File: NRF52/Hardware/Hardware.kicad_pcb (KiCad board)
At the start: 2 copper layers, 33 x 38.1 mm, 81 parts, among them J1 USB_C_Receptacle_USB2.0, J2 1.54 E-INK, J3 Conn_01x04, J4 Battery, Q1 AO3401A, Q2 AO3400A, Q3 AO3400A, Q4 AO3401A, SW1 SW_Push, SW2 SW_Push, SW3 SW_Push, U1 nRF52840, U2 TP4054, U3 BQ27441DRZR-G1A, U4 XC6206PxxxMR, U5 LSM6DS3, U6 DS3231MZ, Y1 32MHz 8pF ±10ppm, Y2 32.768kHz 6pF ±20ppm

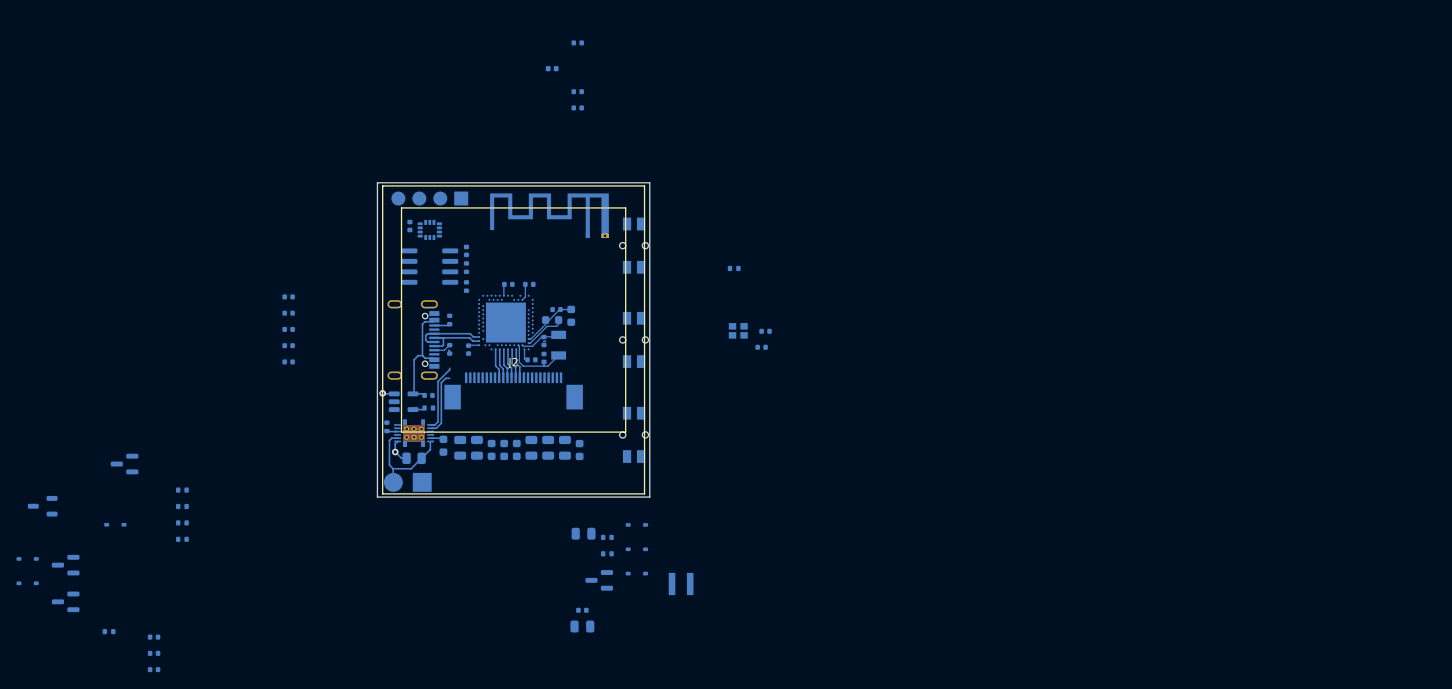
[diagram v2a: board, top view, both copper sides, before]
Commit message: NRF52 hardware as ordered
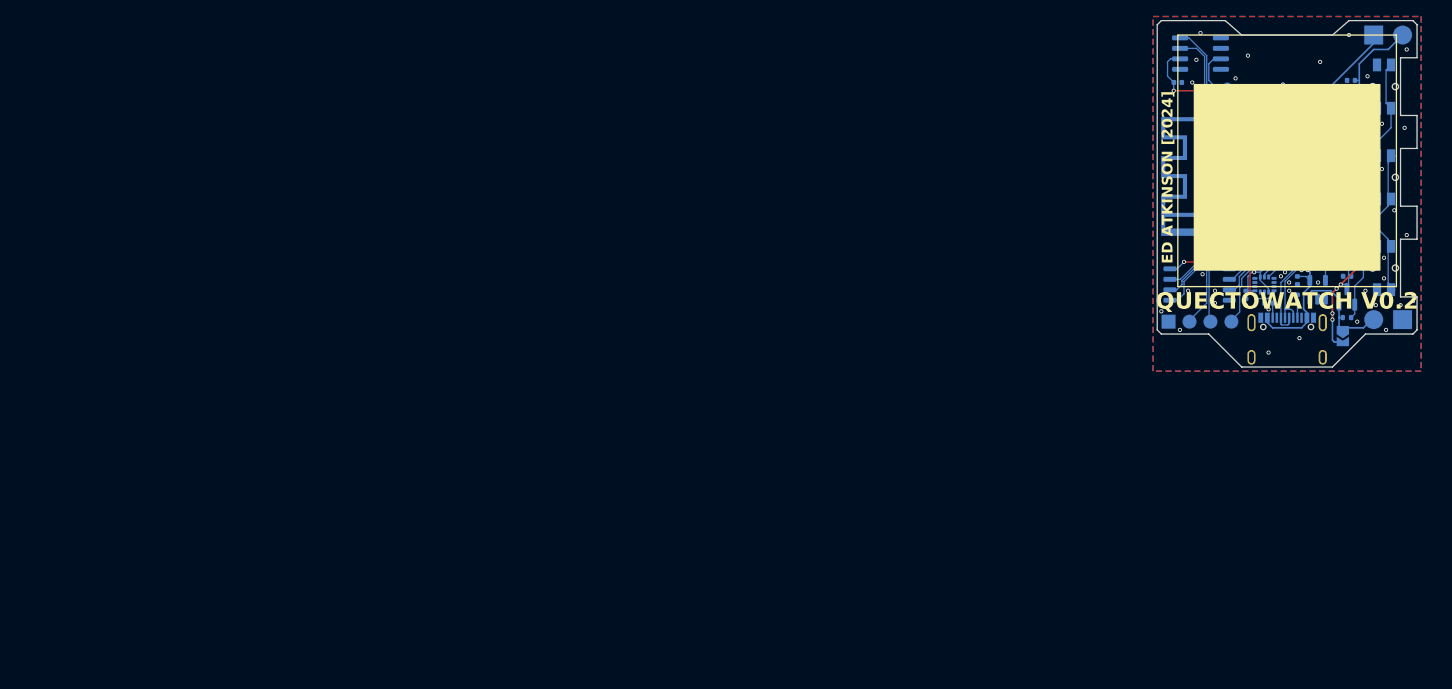
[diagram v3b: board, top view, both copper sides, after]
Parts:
- removed C23, C26, C27, C30: 1u, Capacitor_SMD:C_0603_1608Metric
- removed C24, C25, C28, C29: 4u7, Capacitor_SMD:C_0805_2012Metric
- removed C32: 470n, Capacitor_SMD:C_0603_1608Metric
- removed C33: 100n, Capacitor_SMD:C_0402_1005Metric
- removed D2, D3, D4, D5, D6: 1N5819WS, Diode_SMD:D_SOD-323
- removed L2: 10u, Inductor_SMD:L_Taiyo-Yuden_MD-3030
- removed Q3: AO3400A, Package_TO_SOT_SMD:SOT-23
- removed R12, R13: 10K, Resistor_SMD:R_0402_1005Metric
- added J5: MOTOR, local:Battery Pads, B.Cu at (207.0, 64.0)
- added JP1: SolderJumper_2_Open, Jumper:SolderJumper-2_P1.3mm_Open_TrianglePad1.0x1.5mm, B.Cu at (201.5, 100.5)
- added TP2: LCD_REFRESH, TestPoint:TestPoint_Pad_D1.0mm, B.Cu at (187.5, 70.2)
- added U7: W25Q128JVS, Package_SO:SOIC-8_5.23x5.23mm_P1.27mm, B.Cu at (184.2, 94.2)
- AE1: footprint RF_Antenna:Texas_SWRA117D_2.4GHz_Right -> local:Texas_SWRA117D_2.4GHz_Left
- C19: value 4u7 -> 100n
- C20: value 4u7 -> 100p; footprint Capacitor_SMD:C_0805_2012Metric -> Capacitor_SMD:C_0402_1005Metric
- C21, C22: value 4u7 -> 1u; footprint Capacitor_SMD:C_0805_2012Metric -> Capacitor_SMD:C_0402_1005Metric
- J2: value 1.54 E-INK -> LCD; footprint local:1.54_Epaper_Display -> Connector_FFC-FPC:Molex_54548-1071_1x10-1MP_P0.5mm_Horizontal
- J3: value Conn_01x04 -> PROG
- J4: value Battery -> BAT
- R11: value 1M -> 100K
- R5: value 10K -> 100K
- R6: value 0R47 -> 10K
- R7: value R01 1% -> 10K; footprint Resistor_SMD:R_0805_2012Metric -> Resistor_SMD:R_0402_1005Metric
- U3: value BQ27441DRZR-G1A -> MAX17048; footprint Package_SON:Texas_S-PDSO-N12 -> Package_DFN_QFN:TDFN-8-1EP_2x2mm_P0.5mm_EP0.8x1.2mm
- moved U4 166.1 mm to (202.6, 72.1), turned to -90 degrees
- moved R3 162.1 mm to (202.0, 75.0)
- moved C35 161.8 mm to (202.5, 69.5)
- moved C34 160.0 mm to (204.0, 75.0)
- moved Q4 159.7 mm to (202.0, 95.8), turned to 90 degrees
- moved D1 157.5 mm to (203.2, 77.3), turned to 90 degrees
- moved Q1 151.0 mm to (199.8, 77.2)
- moved R10 142.7 mm to (202.0, 98.2)
- moved R11 132.3 mm to (186.5, 79.8), turned to 0 degrees
- moved C12 126.8 mm to (199.8, 82.2), turned to 0 degrees
- moved C13 125.9 mm to (199.2, 88.0), turned to -90 degrees
- moved C18 121.0 mm to (192.5, 80.5), turned to 90 degrees
- moved C14 120.7 mm to (194.0, 90.0), turned to 0 degrees
- moved J4 120.5 mm to (207.0, 98.5)
- moved R8 118.2 mm to (201.5, 88.2), turned to 0 degrees
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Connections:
- C19 pad 1: +3V3 -> +BATT
- C20 pad 1: Net-(D4-A) -> +3V3
- C20 pad 2: Net-(D2-K) -> GND
- C21 pad 1: /PREVGH -> +3V3
- C22 pad 1: Net-(J2-Pin_4) -> +3V3
- J2 pad 1: unconnected-(J2-Pin_1-Pad1) -> /LCD_SCLK
- J2 pad 10: /EINK_RES -> GND
- J2 pad 2: /GDR -> /LCD_SDI
- J2 pad 3: /RESE -> /LCD_CS
- J2 pad 4: Net-(J2-Pin_4) -> /LCD_REFRESH
- J2 pad 5: Net-(J2-Pin_5) -> +3V3
- J2 pad 6: unconnected-(J2-Pin_6-Pad6) -> +3V3
- J2 pad 7: unconnected-(J2-Pin_7-Pad7) -> +3V3
- J2 pad 8: GND -> +3V3
- J2 pad 9: /EINK_BUSY -> GND
- J3 pad 2: /SWDIO -> /SWDCLK
- J3 pad 3: /SWDCLK -> /SWDIO
- J4 pad 2: Net-(J4-Pin_2) -> Net-(#FLG06-pwr)
- Q1 pad 3: Net-(Q1-D) -> +BATT
- Q2 pad 1: /GDR -> /MOTOR_EN
- Q2 pad 2: /RESE -> GND
- Q2 pad 3: Net-(D4-A) -> Net-(J5-Pin_1)
- Q4 pad 1: Net-(D5-A) -> /POWER_LATCH
- Q4 pad 2: +BATT -> Net-(#FLG06-pwr)
- Q4 pad 3: Net-(Q1-D) -> +BATT
- R10 pad 1: Net-(D5-A) -> /POWER_LATCH
- R10 pad 2: +BATT -> Net-(#FLG06-pwr)
- R11 pad 1: GND -> /MOTOR_EN
- R11 pad 2: /POWER_LATCH -> GND
- R14 pad 2: /SDA -> /RTC_SDA
- R15 pad 2: /SCL -> /RTC_SCL
- R4 pad 1: /~{RESET} -> +3V3
- R4 pad 2: +3V3 -> /IMU_SDA
- R5 pad 1: GND -> +3V3
- R5 pad 2: /GDR -> /LCD_REFRESH
- R6 pad 1: GND -> +3V3
- R6 pad 2: /RESE -> /IMU_SCL
- R7 pad 1: Net-(J4-Pin_2) -> +3V3
- R7 pad 2: +BATT -> /FG_SDA
- R8 pad 1: Net-(U3-BIN) -> +3V3
- R8 pad 2: GND -> /FG_SCL
- SW1 pad 1: GND -> /MENU_BUTTON
- SW1 pad 2: Net-(D5-K) -> GND
- U1 pad A10: unconnected-(U1-AIN5/P0.29-PadA10) -> /LCD_SDI
- U1 pad A12: unconnected-(U1-AIN0/P0.02-PadA12) -> /LCD_SCLK
- U1 pad A14: unconnected-(U1-P1.15-PadA14) -> /RTC_SDA
- U1 pad A16: unconnected-(U1-P1.13-PadA16) -> /RTC_SCL
- U1 pad A20: unconnected-(U1-P1.10-PadA20) -> /MOTOR_EN
- U1 pad A8: unconnected-(U1-AIN7/P0.31-PadA8) -> /LCD_CS
- U1 pad AC11: /POWER_LATCH -> unconnected-(U1-P0.16-PadAC11)
- U1 pad AC9: /DOWN_BUTTON -> unconnected-(U1-P0.14-PadAC9)
- U1 pad AD10: /POWER_BUTTON -> /IMU_SCL
- U1 pad AD12: /VBUS_PRESENT -> /~{RESET}
- U1 pad AD16: /RTC_INT -> unconnected-(U1-P0.20-PadAD16)
- U1 pad AD18: /IMU_INT -> /QSPI_D2
- U1 pad AD20: /SDA -> /QSPI_D1
- U1 pad AD22: /SCL -> /QSPI_CS
- U1 pad AD8: /UP_BUTTON -> /IMU_SDA
- U1 pad B17: /EINK_DC -> unconnected-(U1-P1.12-PadB17)
- U1 pad G1: /EINK_SDI -> /UP_BUTTON
- U1 pad J1: /EINK_SCLK -> /MENU_BUTTON
- U1 pad J24: unconnected-(U1-NFC2/P0.10-PadJ24) -> /QSPI_D3
- U1 pad L1: /EINK_CS -> /DOWN_BUTTON
- U1 pad M2: /RTC_INT -> unconnected-(U1-TRACECLK/P0.07-PadM2)
- U1 pad N1: /EINK_DC -> /POWER_LATCH
- U1 pad R1: /EINK_RES -> /FG_SDA
- U1 pad R24: unconnected-(U1-P1.06-PadR24) -> /QSPI_SCK
- U1 pad U1: /EINK_BUSY -> /FG_SCL
- U1 pad U24: unconnected-(U1-P1.04-PadU24) -> /QSPI_D0
- U1 pad W24: unconnected-(U1-P1.02-PadW24) -> /IMU_INT
- U2 pad 3: +BATT -> Net-(#FLG06-pwr)
- U3 pad 1: /SDA -> GND
- U3 pad 2: /SCL -> +BATT
- U3 pad 3: GND -> +BATT
- U3 pad 4: unconnected-(U3-NC-Pad4) -> GND
- U3 pad 5: Net-(U3-V_{DD}) -> unconnected-(U3-~{ALRT}-Pad5)
- U3 pad 6: Net-(J4-Pin_2) -> GND
- U3 pad 7: +BATT -> /FG_SCL
- U3 pad 8: Net-(J4-Pin_2) -> /FG_SDA
- U3 pad 9: unconnected-(U3-NC-Pad9) -> GND
- U5 pad 13: /SCL -> /IMU_SCL
- U5 pad 14: /SDA -> /IMU_SDA
- U6 pad 2: GND -> unconnected-(U6-VCC-Pad2)
- U6 pad 3: /RTC_INT -> /LCD_REFRESH
- U6 pad 7: /SCL -> /RTC_SCL
- U6 pad 8: /SDA -> /RTC_SDA
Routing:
- net +3V3: track 0.00 -> 136.1 mm, vias 0 -> 14
- net VBUS: track 15.3 -> 49.6 mm, vias 0 -> 4
- net +BATT: track 4.53 -> 37.9 mm, vias 2 -> 6
- net /UP_BUTTON: track 0.00 -> 26.3 mm
- net /RTC_SDA: track 0.00 -> 24.6 mm
- net Net-(J5-Pin_1): track 0.00 -> 24.0 mm, vias 0 -> 2
- net /RTC_SCL: track 0.00 -> 23.6 mm
- net /POWER_LATCH: track 0.00 -> 18.2 mm
- net GND: track 0.45 -> 18.3 mm, vias 0 -> 77
- net /LCD_REFRESH: track 0.00 -> 17.3 mm
- net /DOWN_BUTTON: track 0.00 -> 16.9 mm
- net /MENU_BUTTON: track 0.00 -> 16.5 mm
- net /SWDCLK: track 0.00 -> 16.2 mm
- net /QSPI_D3: track 0.00 -> 15.8 mm
- net /QSPI_D0: track 0.00 -> 15.7 mm
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- added copper zone on B.Cu, net GND
- added copper zone on F.Cu, net GND
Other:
- board size 33 x 38.1 mm -> 31.5 x 42 mm
- board text added: "+ MOT -"
- board text added: "- BAT +"
- board text added: "ED ATKINSON [2024]"
- board text added: "Ed Atkinson 04/2024"
- board text added: "JLCJLCJLCJLC"
- board text added: "PROG"
- board text added: "QUECTOWATCH V0.2"
- board text added: "RESET SWDIO SWDCLK GND"
